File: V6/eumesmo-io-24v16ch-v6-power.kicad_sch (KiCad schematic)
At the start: 51 parts, among them J6 250-202, J7 USB_C_Receptacle_USB2.0, Q1 WPM2015-3/TR, Q2 MMUN2211LT3G, U1 TX4138, U2 SY8089A1AAC

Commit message: Renamed all files to eumesmo branding
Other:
- title: ESP 24V 16xIn/16xOut/1-Wire Module -> eumesmo 24V 16xIn/16xOut/1-Wire Module

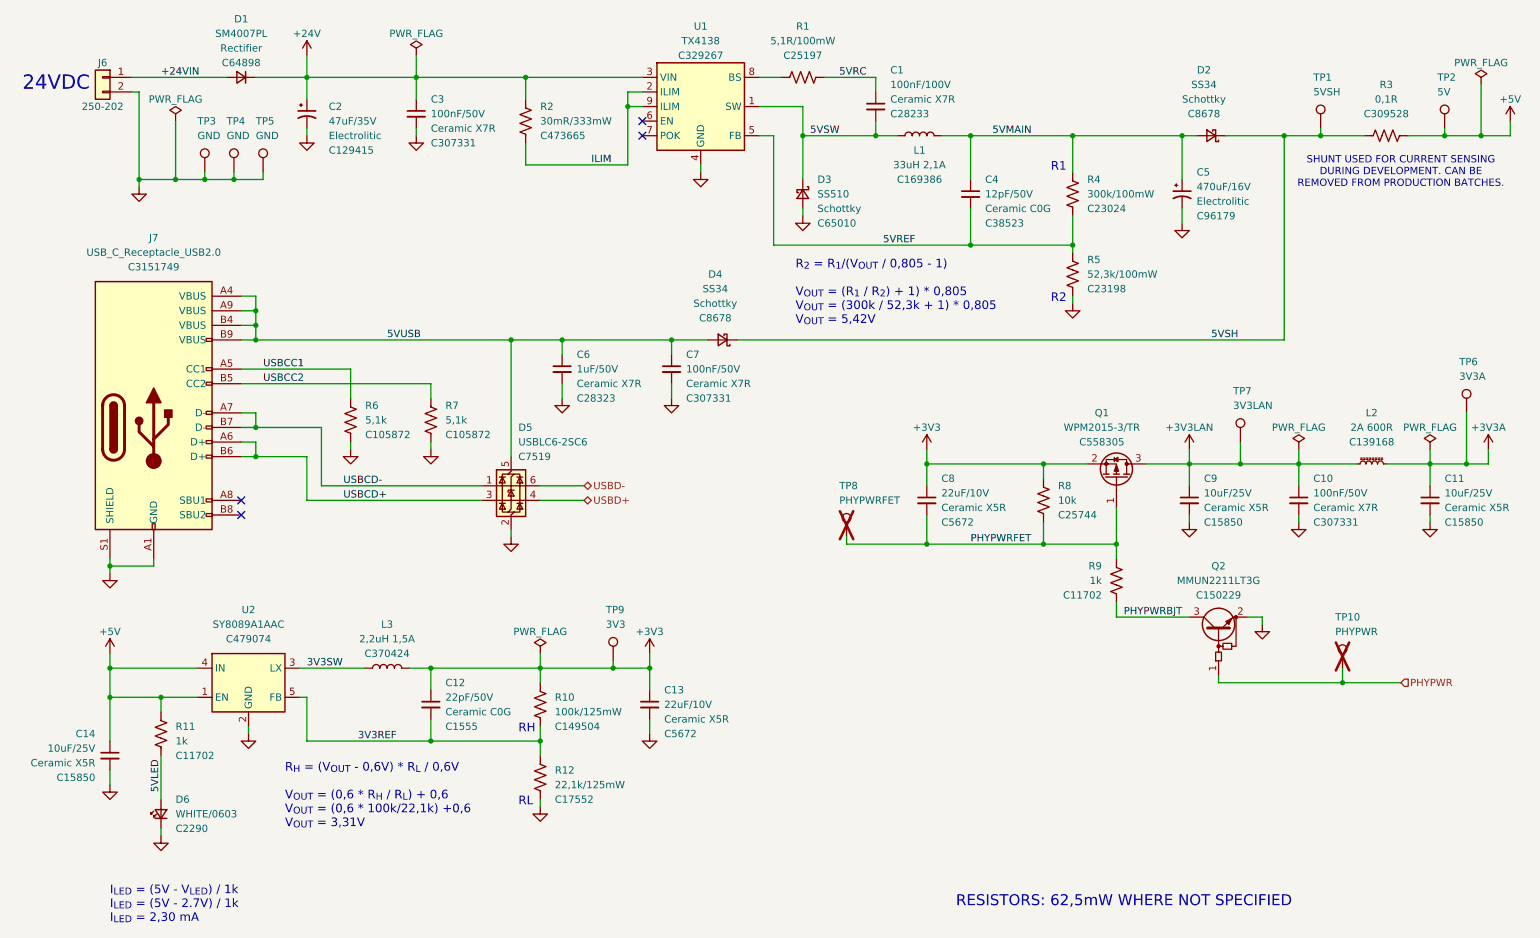
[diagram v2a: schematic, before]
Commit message: Added CPU health LED
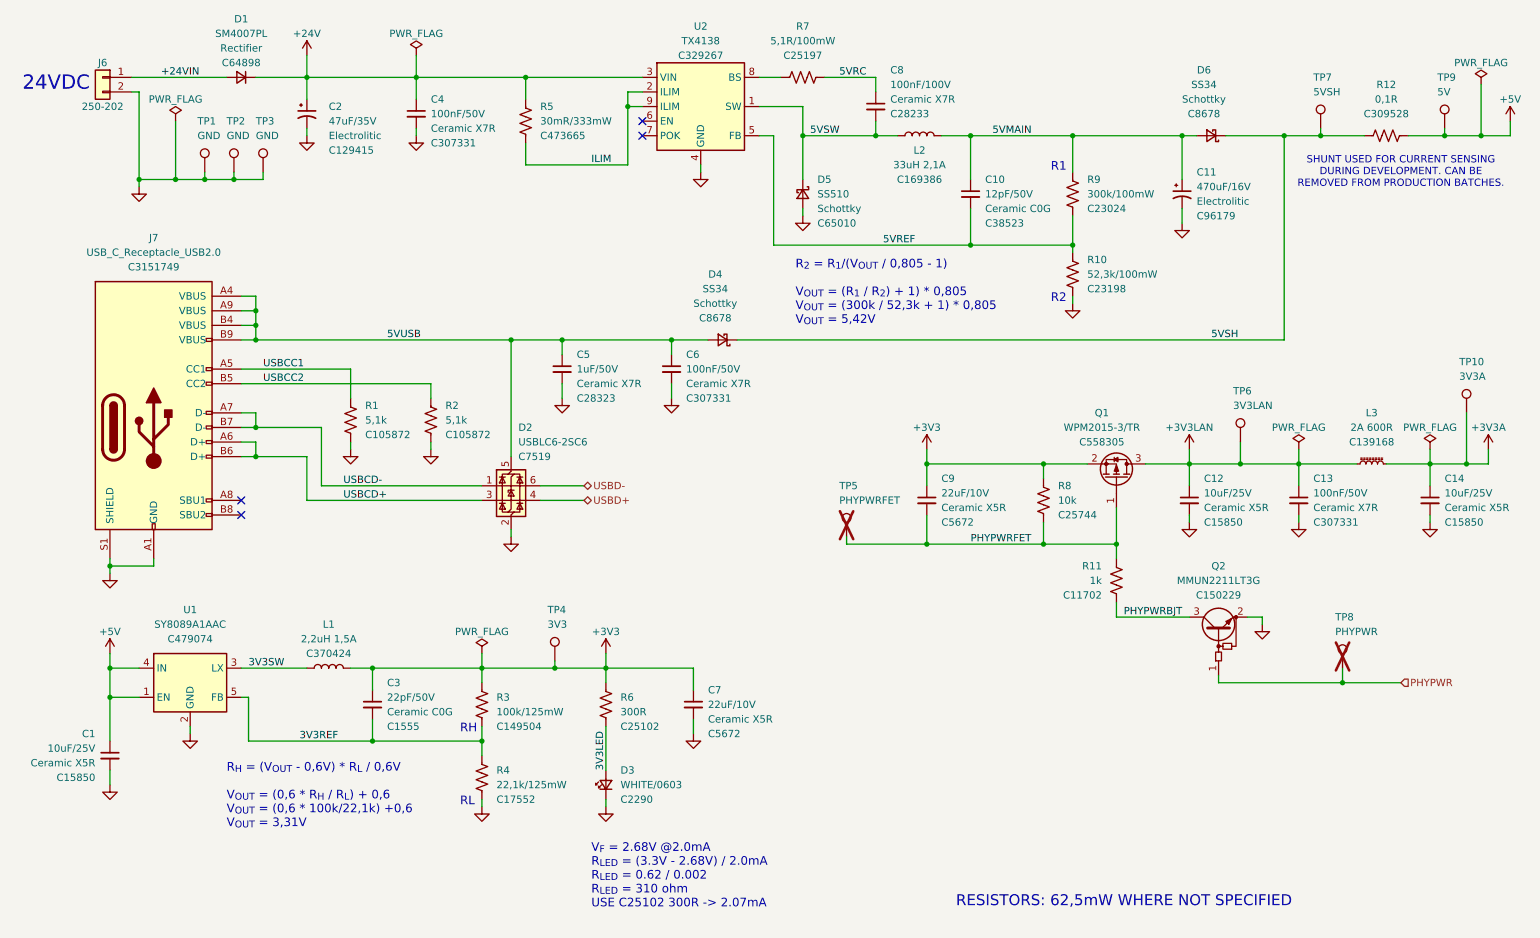
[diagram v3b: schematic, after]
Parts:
- removed D6: WHITE/0603, Tales:LED_0603_1608Metric, symbol Device:LED_Small
- removed R11: 1k, Tales:R_0402_1005Metric, symbol Device:R_US
- added D3: WHITE/0603, Tales:LED_0603_1608Metric, symbol Device:LED_Small
- added R6: 300R, Tales:R_0402_1005Metric, symbol Device:R_US
- renumbered C14 to C1, C4 to C10, C5 to C11, C9 to C12, C10 to C13, C11 to C14, C12 to C3, C3 to C4, C6 to C5, C7 to C6, C13 to C7, C1 to C8, C8 to C9, D5 to D2, D3 to D5, D2 to D6, L3 to L1, L1 to L2, L2 to L3, R6 to R1, R5 to R10, R9 to R11, R3 to R12, R7 to R2, R10 to R3, R12 to R4, R2 to R5, R1 to R7, R4 to R9, TP3 to TP1, TP6 to TP10, TP4 to TP2, TP5 to TP3, TP9 to TP4, TP8 to TP5, TP7 to TP6, TP1 to TP7, TP10 to TP8, TP2 to TP9, U2 to U1, U1 to U2
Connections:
- net +3V3: now also R6.1
- net GND: now also D3.1 (K)
- new net 3V3LED: D3.2 (A), R6.2
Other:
- note added: "V_{F} = 2.68V @2.0mA R_{LED} = (3.3V - 2.68V) / 2.0mA R_{LED} = 0.62 / 0.002 R_{LED} = 310 ohm USE C25102 300R -> 2.07mA"
- note removed: "I_{LED} = (5V - V_{LED}) / 1k I_{LED} = (5V - 2.7V) / 1k I_{LED} = 2,30 mA"
- moved on the sheet: C3, C7, L1, R3, R4, TP4, U1
